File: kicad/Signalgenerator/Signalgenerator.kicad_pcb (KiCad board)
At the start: 2 copper layers, 11 parts, among them U1 LT1354CS8, U2 LT1354CS8, U3 LT1354CS8, U4 LT1354CS8, U5 LT1354CS8, U6 LT1354CS8, U7 LT1354CS8, U8 LT3462ES6-TRPBF

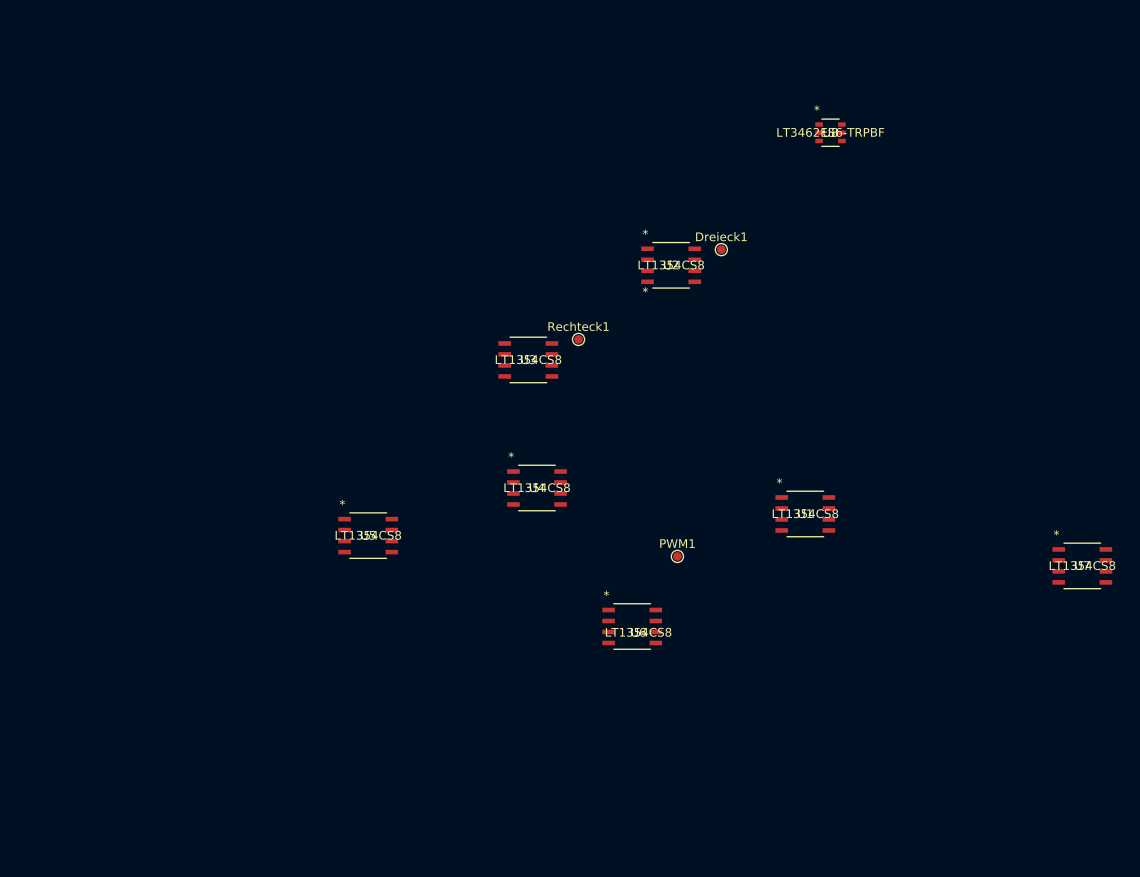
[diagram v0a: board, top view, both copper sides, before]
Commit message: Platine layout angefangen. Probleme mit Überkreuzungen.
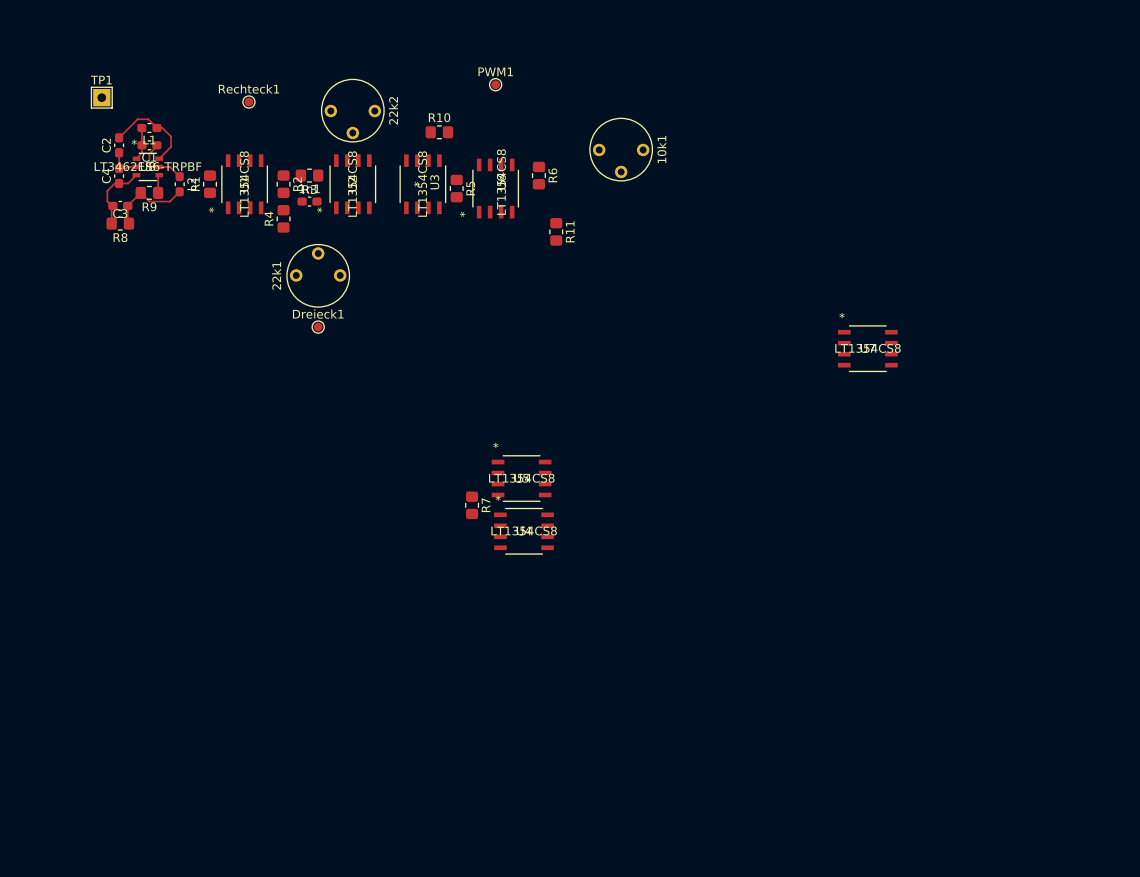
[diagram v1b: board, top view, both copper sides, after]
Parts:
- added 10k1: R_Potentiometer, Potentiometer_THT:Potentiometer_Vishay_T7-YA_Single_Vertical, F.Cu at (81.5, 26.5)
- added 1n1: C, Capacitor_SMD:C_0603_1608Metric_Pad1.08x0.95mm_HandSolder, F.Cu at (48.0, 32.5)
- added 22k1: R_Potentiometer, Potentiometer_THT:Potentiometer_Vishay_T7-YA_Single_Vertical, F.Cu at (51.5, 41.0)
- added 22k2: R_Potentiometer, Potentiometer_THT:Potentiometer_Vishay_T7-YA_Single_Vertical, F.Cu at (50.5, 22.0)
- added C1: 1u, Capacitor_SMD:C_0603_1608Metric_Pad1.08x0.95mm_HandSolder, F.Cu at (29.5, 26.0)
- added C2: 1u, Capacitor_SMD:C_0603_1608Metric_Pad1.08x0.95mm_HandSolder, F.Cu at (26.0, 26.0)
- added C3: 22p, Capacitor_SMD:C_0603_1608Metric_Pad1.08x0.95mm_HandSolder, F.Cu at (26.1, 33.0)
- added C4: 4.7u, Capacitor_SMD:C_0603_1608Metric_Pad1.08x0.95mm_HandSolder, F.Cu at (26.0, 29.5)
- added L1: 22u, Inductor_SMD:L_0603_1608Metric_Pad1.05x0.95mm_HandSolder, F.Cu at (29.5, 24.0)
- added L2: 22u, Inductor_SMD:L_0603_1608Metric_Pad1.05x0.95mm_HandSolder, F.Cu at (33.0, 30.5)
- added R1: 10k, Resistor_SMD:R_0805_2012Metric_Pad1.20x1.40mm_HandSolder, F.Cu at (36.5, 30.5)
- added R10: 1k, Resistor_SMD:R_0805_2012Metric_Pad1.20x1.40mm_HandSolder, F.Cu at (63.0, 24.5)
- added R11: 1k, Resistor_SMD:R_0805_2012Metric_Pad1.20x1.40mm_HandSolder, F.Cu at (76.5, 36.0)
- added R2: 10k, Resistor_SMD:R_0805_2012Metric_Pad1.20x1.40mm_HandSolder, F.Cu at (45.0, 30.5)
- added R3: 220, Resistor_SMD:R_0805_2012Metric_Pad1.20x1.40mm_HandSolder, F.Cu at (48.0, 29.5)
- added R4: 10k, Resistor_SMD:R_0805_2012Metric_Pad1.20x1.40mm_HandSolder, F.Cu at (45.0, 34.5)
- added R5: 1k, Resistor_SMD:R_0805_2012Metric_Pad1.20x1.40mm_HandSolder, F.Cu at (65.0, 31.0)
- added R6: 1M, Resistor_SMD:R_0805_2012Metric_Pad1.20x1.40mm_HandSolder, F.Cu at (74.5, 29.5)
- added R7: 4.7k, Resistor_SMD:R_0805_2012Metric_Pad1.20x1.40mm_HandSolder, F.Cu at (66.8, 67.6)
- added R8: 71.1k, Resistor_SMD:R_0805_2012Metric_Pad1.20x1.40mm_HandSolder, F.Cu at (26.1, 35.0)
- added R9: 10k, Resistor_SMD:R_0805_2012Metric_Pad1.20x1.40mm_HandSolder, F.Cu at (29.5, 31.5)
- added TP1: TestPoint, TestPoint:TestPoint_THTPad_2.0x2.0mm_Drill1.0mm, F.Cu at (24.0, 20.5)
- moved U8 79.0 mm to (29.3, 28.5)
- moved U1 75.1 mm to (40.5, 30.5), turned to 90 degrees
- moved PWM1 58.4 mm to (69.5, 19.0)
- moved U6 53.0 mm to (69.5, 31.0), turned to 90 degrees
- moved Dreieck1 47.4 mm to (49.0, 47.0)
- moved Rechteck1 46.9 mm to (41.0, 21.0)
- moved U2 37.9 mm to (53.0, 30.5), turned to 90 degrees
- moved U7 35.3 mm to (112.5, 49.5)
- moved U3 23.7 mm to (61.1, 30.5), turned to 90 degrees
- moved U5 18.9 mm to (72.5, 64.5)
- moved U4 5.22 mm to (72.8, 70.6)
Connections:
- U1 pad 1: GND -> unconnected-(U1-NULL-Pad1)
- U1 pad 8: GND -> unconnected-(U1-NULL-Pad8)
- U2 pad 1: GND -> unconnected-(U2-NULL-Pad1)
- U2 pad 3: unconnected-(U2-+IN-Pad3) -> Net-(U2-+IN)
- U2 pad 8: GND -> unconnected-(U2-NULL-Pad8)
- U6 pad 2: unconnected-(U6--IN-Pad2) -> Net-(U6--IN)
- U8 pad 1: unconnected-(U8-SW-Pad1) -> Net-(U8-SW)
- U8 pad 2: unconnected-(U8-GND-Pad2) -> Net-(U8-GND)
- U8 pad 3: unconnected-(U8-FB-Pad3) -> Ub-
- U8 pad 4: unconnected-(U8-SDREF-Pad4) -> Net-(U8-SDREF)
- U8 pad 5: unconnected-(U8-D-Pad5) -> Net-(U8-D)
- U8 pad 6: unconnected-(U8-VIN-Pad6) -> Ub+
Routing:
- net Ub+: track 0.00 -> 11.3 mm
- net Net-(C3-Pad1): track 0.00 -> 9.61 mm
- net Ub-: track 0.00 -> 7.93 mm
- net Net-(U8-D): track 0.00 -> 6.82 mm
- net Net-(U8-GND): track 0.00 -> 4.17 mm
- net Net-(U8-SW): track 0.00 -> 3.82 mm
- net Net-(U8-SDREF): track 0.00 -> 2.10 mm

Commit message: kleine änderungen
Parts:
- added C5: 2.2u, Capacitor_SMD:C_0603_1608Metric_Pad1.08x0.95mm_HandSolder, F.Cu at (24.5, 29.5)
- C4: value 4.7u -> 2.2u
- R4: value 10k -> 1k
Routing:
- net Net-(U8-GND): track 4.17 -> 5.69 mm
- net Ub-: track 7.93 -> 9.20 mm
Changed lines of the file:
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@@
 		(embedded_fonts no)
+	)
+	(footprint "Capacitor_SMD:C_0603_1608Metric_Pad1.08x0.95mm_HandSolder"
+		(layer "F.Cu")
+		(at 24.5 29.5 90)
+		(descr "Capacitor SMD 0603 (1608 Metric), square (rectangular) end terminal, IPC-7351 nominal with elongated pad for handsoldering. (Body size source: IPC-SM-782 page 76, https://www.pcb-3d.com/wordpress/wp-content/uploads/ipc-sm-782a_amendment_1_and_2.pdf), generated with kicad-footprint-generator")
+		(tags "capacitor handsolder")
+		(property "Reference" "C5"
+			(at 0 -1.43 90)
+			(layer "F.SilkS")
+			(effects
+				(font
+					(size 1 1)
+					(thickness 0.15)
+				)
+			)
+		)
+		(property "Value" "2.2u"
+			(at 0 1.43 90)
+			(layer "F.Fab")
+			(effects
+				(font
+					(size 1 1)
+					(thickness 0.15)
+				)
+			)
+		)
+		(property "Datasheet" "~"
+			(at 0 0 90)
+			(layer "F.Fab")
+			(hide yes)
+			(effects
+				(font
+					(size 1.27 1.27)
+					(thickness 0.15)
+				)
+			)
+		)
+		(property "Description" "Unpolarized capacitor"
+			(at 0 0 90)
+			(layer "F.Fab")
+			(hide yes)
+			(effects
+				(font
+					(size 1.27 1.27)
+					(thickness 0.15)
+				)
+			)
+		)
+		(property ki_fp_filters "C_*")
+		(sheetname "/spannungsversorgung/")
+		(sheetfile "untitled.kicad_sch")
+		(attr smd)
+		(fp_line
+			(start -0.146267 -0.51)
+			(end 0.146267 -0.51)
+			(stroke
+				(width 0.12)
+				(type solid)
+			)
+			(layer "F.SilkS")
+		)
+		(fp_line
+			(start -0.146267 0.51)
+			(end 0.146267 0.51)
+			(stroke
+				(width 0.12)
+				(type solid)
+			)
+			(layer "F.SilkS")
+		)
+		(fp_rect
+			(start -1.65 -0.73)
+			(end 1.65 0.73)
+			(stroke
+				(width 0.05)
+				(type solid)
+			)
+			(fill no)
+			(layer "F.CrtYd")
+		)
+		(fp_rect
+			(start -0.8 -0.4)
+			(end 0.8 0.4)
+			(stroke
+				(width 0.1)
+				(type solid)
+			)
+			(fill no)
+			(layer "F.Fab")
+		)
+		(fp_text user "${REFERENCE}"
+			(at 0 0 90)
+			(layer "F.Fab")
+			(effects
+				(font
+					(size 0.4 0.4)
+					(thickness 0.06)
+				)
+			)
+		)
+		(pad "1" smd roundrect
+			(at -0.8625 0 90)
+			(size 1.075 0.95)
+			(layers "F.Cu" "F.Mask" "F.Paste")
+			(roundrect_rratio 0.25)
+			(net 7 "Ub-")
+			(pintype "passive")
+		)
+		(pad "2" smd roundrect
+			(at 0.8625 0 90)
+			(size 1.075 0.95)
+			(layers "F.Cu" "F.Mask" "F.Paste")
+			(roundrect_rratio 0.25)
+			(net 37 "Net-(U8-GND)")
+			(pintype "passive")
+		)
+		(embedded_fonts no)
+		(model "${KICAD9_3DMODEL_DIR}/Capacitor_SMD.3dshapes/C_0603_1608Metric.step"
+			(offset
+				(xyz 0 0 0)
+			)
+			(scale
+				(xyz 1 1 1)
+			)
+			(rotate
+				(xyz 0 0 0)
+			)
+		)
 	)
 	(footprint "Resistor_SMD:R_0805_2012Metric_Pad1.20x1.40mm_HandSolder"
@@
 			)
 		)
-		(property "Value" "4.7u"
+		(property "Value" "2.2u"
 			(at 0 1.43 90)
 			(layer "F.Fab")
@@
 			)
 		)
-		(property "Value" "10k"
+		(property "Value" "1k"
 			(at 0 1.65 90)
 			(layer "F.Fab")
@@
 	)
 	(segment
+		(start 24.5 30.3625)
+		(end 24.5 31.137499)
+		(width 0.2)
+		(layer "F.Cu")
+		(net 7)
+	)
+	(segment
 		(start 27.037502 30.412499)
 		(end 28 29.450001)
@@
 	)
 	(segment
+		(start 24.5 31.137499)
+		(end 24.6375 31.274999)
+		(width 0.2)
+		(layer "F.Cu")
+		(net 7)
+	)
+	(segment
+		(start 24.5 30.3625)
+		(end 25.950001 30.3625)
+		(width 0.2)
+		(layer "F.Cu")
+		(net 7)
+	)
+	(segment
 		(start 24.6375 32.5)
 		(end 24.6375 31.274999)
@@
 	)
 	(segment
+		(start 25.950001 30.3625)
+		(end 26 30.412499)
+		(width 0.2)
+		(layer "F.Cu")
+		(net 7)
+	)
+	(segment
 		(start 27.037502 30.412499)
 		(end 26 30.412499)
@@
 	)
 	(segment
-		(start 24.6375 31.274999)
-		(end 25.5 30.412499)
-		(width 0.2)
-		(layer "F.Cu")
-		(net 7)
-	)
-	(segment
 		(start 25.1375 33)
 		(end 24.6375 32.5)
@@
 		(width 0.2)
 		(layer "F.Cu")
+		(net 37)
+	)
+	(segment
+		(start 24.5 28.6375)
+		(end 25.950001 28.6375)
+		(width 0.2)
+		(layer "F.Cu")
+		(net 37)
+	)
+	(segment
+		(start 25.950001 28.6375)
+		(end 26 28.687499)
+		(width 0.2)
+		(layer "F.Cu")

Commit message: layout zwischenstand
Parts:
- added C10: 0.1u, Capacitor_SMD:C_0603_1608Metric_Pad1.08x0.95mm_HandSolder, F.Cu at (39.1, 100.5)
- added C11: 0.1u, Capacitor_SMD:C_0603_1608Metric_Pad1.08x0.95mm_HandSolder, F.Cu at (39.1, 103.0)
- added C12: 0.1u, Capacitor_SMD:C_0603_1608Metric_Pad1.08x0.95mm_HandSolder, F.Cu at (48.5, 26.0)
- added C13: 0.1u, Capacitor_SMD:C_0603_1608Metric_Pad1.08x0.95mm_HandSolder, F.Cu at (83.1, 37.0)
- added C14: 0.1u, Capacitor_SMD:C_0603_1608Metric_Pad1.08x0.95mm_HandSolder, F.Cu at (43.5, 98.0)
- added C15: 0.1u, Capacitor_SMD:C_0603_1608Metric_Pad1.08x0.95mm_HandSolder, F.Cu at (43.5, 100.5)
- added C16: 0.1u, Capacitor_SMD:C_0603_1608Metric_Pad1.08x0.95mm_HandSolder, F.Cu at (43.5, 103.0)
- added C17: 0.1u, Capacitor_SMD:C_0603_1608Metric_Pad1.08x0.95mm_HandSolder, F.Cu at (42.5, 36.0)
- added C18: 0.1u, Capacitor_SMD:C_0603_1608Metric_Pad1.08x0.95mm_HandSolder, F.Cu at (39.8, 25.0)
- added C19: 0.1u, Capacitor_SMD:C_0603_1608Metric_Pad1.08x0.95mm_HandSolder, F.Cu at (47.8, 98.0)
- added C20: 0.1u, Capacitor_SMD:C_0603_1608Metric_Pad1.08x0.95mm_HandSolder, F.Cu at (47.8, 100.5)
- added C21: 0.1u, Capacitor_SMD:C_0603_1608Metric_Pad1.08x0.95mm_HandSolder, F.Cu at (23.0, 29.5)
- added C22: 1n, Capacitor_SMD:C_0603_1608Metric_Pad1.08x0.95mm_HandSolder, F.Cu at (49.5, 40.0)
- added C23: 100p, Capacitor_SMD:C_0603_1608Metric_Pad1.08x0.95mm_HandSolder, F.Cu at (49.5, 38.5)
- added C6: 10n, Capacitor_SMD:C_0603_1608Metric_Pad1.08x0.95mm_HandSolder, F.Cu at (72.6, 74.5)
- added C7: 0.1u, Capacitor_SMD:C_0603_1608Metric_Pad1.08x0.95mm_HandSolder, F.Cu at (52.0, 35.5)
- added C8: 0.1u, Capacitor_SMD:C_0603_1608Metric_Pad1.08x0.95mm_HandSolder, F.Cu at (79.5, 21.5)
- added C9: 0.1u, Capacitor_SMD:C_0603_1608Metric_Pad1.08x0.95mm_HandSolder, F.Cu at (39.1, 98.0)
- added D1: D, Diode_THT:D_A-405_P2.54mm_Vertical_AnodeUp, F.Cu at (48.5, 23.0)
- added J1: Conn_01x01, Connector_PinHeader_2.54mm:PinHeader_1x01_P2.54mm_Vertical, F.Cu at (21.5, 25.0)
- added J2: Conn_01x01, Connector_PinHeader_2.54mm:PinHeader_1x01_P2.54mm_Vertical, F.Cu at (19.0, 29.5)
- added R12: 1k, Resistor_SMD:R_0805_2012Metric_Pad1.20x1.40mm_HandSolder, F.Cu at (87.0, 97.0)
- added R13: 10k, Resistor_SMD:R_0805_2012Metric_Pad1.20x1.40mm_HandSolder, F.Cu at (72.5, 76.5)
- added R14: 0, Resistor_SMD:R_0805_2012Metric_Pad1.20x1.40mm_HandSolder, F.Cu at (70.5, 25.0)
- added R16: 0, Resistor_SMD:R_0805_2012Metric_Pad1.20x1.40mm_HandSolder, F.Cu at (66.5, 38.5)
- added RV1: R_Potentiometer, Potentiometer_THT:Potentiometer_Vishay_T7-YA_Single_Vertical, F.Cu at (98.7, 95.6)
- added RV2: R_Potentiometer, Potentiometer_THT:Potentiometer_Vishay_T7-YA_Single_Vertical, F.Cu at (98.7, 104.1)
- added SW1: OS103011MS8QP1, footprints:OS103011MS8QP1, F.Cu at (56.0, 41.5)
- added SW2: SW_DPDT_x2, Button_Switch_THT:SW_Slide_SPDT_Straight_CK_OS102011MS2Q, F.Cu at (56.0, 22.5)
- added SW3: OS103011MS8QP1, footprints:OS103011MS8QP1, F.Cu at (111.9, 92.4)
- C24: renamed from 1n1; value C -> 10n
- moved U7 19.7 mm to (104.7, 31.4)
- moved Dreieck1 17.8 mm to (63.0, 36.0)
- moved R11 12.0 mm to (88.5, 37.0)
- moved 22k1 11.7 mm to (40.5, 45.0), turned to 0 degrees
- moved R10 11.5 mm to (74.5, 24.0)
- moved 10k1 9.19 mm to (90.4, 24.5)
- moved C24 9.12 mm to (49.5, 41.5), turned to 180 degrees
- moved R5 8.50 mm to (73.5, 31.0)
- moved R6 8.50 mm to (83.0, 29.5)
- moved U6 8.50 mm to (78.0, 31.0)
- moved Rechteck1 8.20 mm to (46.0, 27.5)
- moved R3 7.81 mm to (42.0, 24.5), turned to -90 degrees
- moved 22k2 6.73 mm to (45.5, 17.5)
- moved R4 4.92 mm to (40.5, 36.5)
- moved PWM1 4.03 mm to (73.5, 18.5)
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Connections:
- 22k1 pad 2: Net-(U2-OUT) -> Net-(U2--IN)
- 22k2 pad 2: Net-(U2-+IN) -> Net-(SW2A-A)
- C2 pad 1: Net-(U8-GND) -> GND
- C24 pad 1: Net-(U2-OUT) -> Net-(C24-Pad1)
- C4 pad 2: Net-(U8-GND) -> GND
- C5 pad 2: Net-(U8-GND) -> GND
- U2 pad 3: Net-(U2-+IN) -> Net-(SW2A-B)
- U3 pad 3: Net-(U2-OUT) -> Net-(U3-+IN)
- U4 pad 3: unconnected-(U4-+IN-Pad3) -> GND
- U4 pad 6: unconnected-(U4-OUT-Pad6) -> Net-(U4-OUT)
- U7 pad 2: unconnected-(U7--IN-Pad2) -> Net-(U7--IN)
- U7 pad 3: unconnected-(U7-+IN-Pad3) -> Net-(U7-+IN)
- U7 pad 6: unconnected-(U7-OUT-Pad6) -> Net-(U7-OUT)
- U8 pad 2: Net-(U8-GND) -> GND
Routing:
- net Ub+: track 11.3 -> 41.2 mm
- net Ub-: track 9.20 -> 33.7 mm
- net GND: track 0.00 -> 15.8 mm
- net Net-(U1-OUT): track 0.00 -> 7.67 mm
- net Net-(U1-+IN): track 0.00 -> 7.12 mm
- net Net-(U8-GND): track 5.69 -> 0.00 mm
- net Net-(U1--IN): track 0.41 -> 5.91 mm
- net Net-(D1-A): track 0.00 -> 0.71 mm

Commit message: rechteck dreieck hässlich
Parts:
- added R15: 0, Resistor_SMD:R_0805_2012Metric_Pad1.20x1.40mm_HandSolder, F.Cu at (49.0, 35.5)
- added R17: 0, Resistor_SMD:R_0805_2012Metric_Pad1.20x1.40mm_HandSolder, F.Cu at (54.5, 27.0)
- moved R5 21.5 mm to (61.0, 48.5)
- moved U6 18.8 mm to (81.5, 49.5)
- moved R16 12.3 mm to (61.0, 27.5)
- moved SW1 10.0 mm to (55.5, 31.5), turned to 0 degrees
- moved U3 8.50 mm to (70.0, 34.5)
- moved SW2 4.95 mm to (52.5, 19.0)
- moved C23 3.16 mm to (50.5, 41.5)
- moved C24 3.16 mm to (50.5, 38.5)
- moved 22k2 2.04 mm to (45.0, 19.5), turned to 0 degrees
- moved C22 1.00 mm to (50.5, 40.0)
- moved D1 1.00 mm to (47.5, 23.0)
- moved J2 0.71 mm to (19.5, 29.0)
- moved C7 0.50 mm to (52.0, 36.0)
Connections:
- SW1 pad 2: Net-(U2-OUT) -> Net-(R17-Pad1)
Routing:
- net GND: track 15.8 -> 71.8 mm
- net Net-(U2--IN): track 0.00 -> 15.7 mm
- net Net-(SW2A-B): track 0.00 -> 15.7 mm
- net Net-(R17-Pad1): track 0.00 -> 10.0 mm
- net Net-(C24-Pad1): track 0.00 -> 9.38 mm
- net Ub-: track 33.7 -> 41.5 mm
- net Net-(D1-A): track 0.71 -> 7.12 mm
- net Net-(U2-OUT): track 0.00 -> 6.00 mm
- net Net-(C22-Pad2): track 0.00 -> 5.17 mm
- net Net-(SW2A-A): track 0.00 -> 5.14 mm
- net Net-(C23-Pad2): track 0.00 -> 4.97 mm
- net Net-(D1-K): track 0.00 -> 4.95 mm
- net Net-(22k1-Pad3): track 0.00 -> 2.48 mm

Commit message: kleine änderungen
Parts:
- removed TP1: TestPoint, TestPoint:TestPoint_THTPad_2.0x2.0mm_Drill1.0mm
- moved C20 44.7 mm to (80.5, 70.0)
- moved C10 20.5 mm to (48.0, 82.0)
- moved C14 20.5 mm to (52.4, 79.5)
- moved C15 20.5 mm to (52.4, 82.0)
- moved C19 20.5 mm to (56.7, 79.5)
- moved C9 20.5 mm to (48.0, 79.5)
- moved C11 20.5 mm to (48.0, 84.5)
- moved C16 20.5 mm to (52.4, 84.5)
- moved Dreieck1 16.5 mm to (63.0, 19.5)
- moved J2 7.86 mm to (21.2, 36.7)
- moved U3 6.58 mm to (63.5, 33.5)
- moved R14 4.12 mm to (69.5, 21.0)
- moved 22k1 4.05 mm to (42.5, 48.6)
- moved 22k2 3.91 mm to (43.7, 23.2)
- moved C12 3.91 mm to (47.2, 29.7)
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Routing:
- net GND: track 71.8 -> 97.1 mm
- net Net-(U2--IN): track 15.7 -> 12.4 mm
- net Ub+: track 41.2 -> 38.3 mm
- net Net-(U2-OUT): track 6.00 -> 3.63 mm
- net Net-(R17-Pad1): track 10.0 -> 12.4 mm
- net Net-(D1-K): track 4.95 -> 6.82 mm
- net Net-(SW2A-B): track 15.7 -> 17.5 mm
- net Net-(22k1-Pad3): track 2.48 -> 4.28 mm
- net Ub-: track 41.5 -> 40.3 mm

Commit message: aktueller stand
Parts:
- added R18: 0, Resistor_SMD:R_0805_2012Metric_Pad1.20x1.40mm_HandSolder, F.Cu at (46.5, 42.0)
- moved C16 55.1 mm to (107.3, 80.4)
- moved U7 53.1 mm to (105.0, 84.5)
- moved C13 49.4 mm to (98.8, 83.9)
- moved C14 46.5 mm to (62.0, 34.0), turned to 180 degrees
- moved C9 40.8 mm to (53.0, 39.0), turned to -90 degrees
- moved C15 38.4 mm to (80.6, 108.0)
- moved PWM1 38.1 mm to (54.5, 51.5)
- moved C8 37.7 mm to (58.0, 52.5)
- moved C19 36.5 mm to (57.4, 43.0), turned to 180 degrees
- moved R6 33.7 mm to (54.5, 47.5), turned to 90 degrees
- moved R11 26.6 mm to (62.5, 42.5), turned to 0 degrees
- moved Dreieck1 25.9 mm to (52.0, 43.0)
- moved 10k1 24.7 mm to (68.0, 35.0), turned to 180 degrees
- moved C20 24.7 mm to (56.0, 73.0), turned to 180 degrees
- moved U6 23.1 mm to (58.5, 47.5), turned to -90 degrees
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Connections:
- 22k1 pad 2: Net-(U2--IN) -> Net-(22k1-Pad2)
- C22 pad 1: Net-(U2--IN) -> Net-(22k1-Pad2)
- C23 pad 1: Net-(U2--IN) -> Net-(22k1-Pad2)
- C24 pad 2: Net-(U2--IN) -> Net-(22k1-Pad2)
- Dreieck1 pad 1: Net-(U2-OUT) -> Net-(U5-+IN)
- R16 pad 2: Net-(U2-OUT) -> Net-(U5-+IN)
- R17 pad 1: Net-(R17-Pad1) -> Net-(U5-+IN)
- SW1 pad 2: Net-(R17-Pad1) -> Net-(U5-+IN)
- SW3 pad 3: Net-(U2-OUT) -> Net-(U5-+IN)
- U5 pad 3: Net-(U2-OUT) -> Net-(U5-+IN)
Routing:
- net GND: track 97.1 -> 78.7 mm
- net Net-(U5-+IN): track 0.00 -> 16.1 mm
- net Ub+: track 38.3 -> 52.2 mm
- net Net-(R17-Pad1): track 12.4 -> 0.00 mm
- net Ub-: track 40.3 -> 51.6 mm
- net Net-(22k1-Pad2): track 0.00 -> 11.2 mm
- net Net-(U2--IN): track 12.4 -> 4.86 mm
- net Net-(U3--IN): track 0.00 -> 5.97 mm
- net Net-(U3-+IN): track 0.00 -> 5.50 mm
- net Net-(U2-OUT): track 3.63 -> 9.12 mm
- net Net-(C24-Pad1): track 9.38 -> 4.18 mm
- net Net-(U1-OUT): track 7.67 -> 10.3 mm
- net Net-(SW2A-A): track 5.04 -> 7.43 mm
- net Net-(D1-A): track 7.12 -> 9.41 mm
- net Net-(C22-Pad2): track 5.17 -> 3.05 mm
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
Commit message: schaltplan angepasst
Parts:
- removed C11, C13, C15, C17, C19: 0.1u, Capacitor_SMD:C_0603_1608Metric_Pad1.08x0.95mm_HandSolder
- added TP1: TestPoint, TestPoint:TestPoint_THTPad_2.0x2.0mm_Drill1.0mm, F.Cu at (93.0, 83.0)
- C7, C9: value 0.1u -> C
- moved C9 38.0 mm to (15.6, 32.0), turned to 0 degrees
- moved C7 36.5 mm to (15.6, 29.5), turned to 0 degrees
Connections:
- C10 pad 1: GND -> Ub-
- C12 pad 1: GND -> Ub-
- C14 pad 1: GND -> Ub-
- C16 pad 1: GND -> Ub-
- C18 pad 1: GND -> Ub-
- C20 pad 1: GND -> Ub-
- C7 pad 1: Ub- -> Ub+
- C7 pad 2: GND -> Ub-
- C8 pad 1: GND -> Ub-
- C9 pad 1: Ub- -> Ub+
- C9 pad 2: GND -> Ub-
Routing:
- net GND: track 78.7 -> 36.6 mm
- net Ub+: track 52.2 -> 39.7 mm
- net Ub-: track 51.6 -> 52.1 mm
